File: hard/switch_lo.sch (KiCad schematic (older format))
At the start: 4 parts

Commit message: pc format refactor wip
@lukekaese leds still need to be attenuated
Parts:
- gave numbers to parts that had none: 4

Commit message: layouting update
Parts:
- R97: renamed from R99; footprint Resistor_SMD:R_0603_1608Metric -> Resistor_SMD:R_1210_3225Metric
- R98: renamed from R97; footprint Resistor_SMD:R_0603_1608Metric -> Resistor_SMD:R_0402_1005Metric
- R99: renamed from R98; footprint Resistor_SMD:R_0603_1608Metric -> Resistor_SMD:R_0402_1005Metric

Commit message: driver nmos update
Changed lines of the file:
@@
 $Descr A4 11693 8268
 encoding utf-8
-Sheet 36 69
+Sheet 39 69
 Title ""
 Date ""
@@
 AR Path="/6053C67A/DAE5EF41/6879FA6E" Ref="M95"  Part="1"
 AR Path="/6053C67A/DAE5EF45/6879FA6E" Ref="M96"  Part="1"
-F 0 "M65" H 6078 4300 50  0000 L CNN
+F 0 "M68" H 6078 4300 50  0000 L CNN
 F 1 "IRLML0030TRPBF" H 6078 4255 50  0001 L CNN
 F 2 "Package_TO_SOT_SMD:SOT-23" H 6750 4300 50  0001 C CNN
@@
 AR Path="/6053C67A/DAE5EF41/6879FA74" Ref="R189"  Part="1"
 AR Path="/6053C67A/DAE5EF45/6879FA74" Ref="R192"  Part="1"
-F 0 "R99" H 5720 4546 50  0000 L CNN
+F 0 "R108" H 5720 4546 50  0000 L CNN
 F 1 "470K" H 5720 4455 50  0000 L CNN
 F 2 "Resistor_SMD:R_0402_1005Metric" V 5580 4500 50  0001 C CNN
@@
 AR Path="/6053C67A/DAE5EF41/6879FA7A" Ref="R188"  Part="1"
 AR Path="/6053C67A/DAE5EF45/6879FA7A" Ref="R191"  Part="1"
-F 0 "R98" V 5243 4300 50  0000 C CNN
+F 0 "R107" V 5243 4300 50  0000 C CNN
 F 1 "1K8" V 5334 4300 50  0000 C CNN
 F 2 "Resistor_SMD:R_0402_1005Metric" V 5380 4300 50  0001 C CNN
@@
 AR Path="/6053C67A/DAE5EF41/6879FA80" Ref="#PWR0174"  Part="1"
 AR Path="/6053C67A/DAE5EF45/6879FA80" Ref="#PWR0176"  Part="1"
-F 0 "#PWR0114" H 5650 4450 50  0001 C CNN
+F 0 "#PWR0120" H 5650 4450 50  0001 C CNN
 F 1 "GND" H 5655 4527 50  0000 C CNN
 F 2 "" H 5650 4700 50  0001 C CNN
@@
 AR Path="/6053C67A/DAE5EF41/6879FA89" Ref="#PWR0175"  Part="1"
 AR Path="/6053C67A/DAE5EF45/6879FA89" Ref="#PWR0177"  Part="1"
-F 0 "#PWR0115" H 6000 4450 50  0001 C CNN
+F 0 "#PWR0121" H 6000 4450 50  0001 C CNN
 F 1 "GND" H 6005 4527 50  0000 C CNN
 F 2 "" H 6000 4700 50  0001 C CNN
@@
 AR Path="/6053C67A/DAE5EF41/6879FB77" Ref="R187"  Part="1"
 AR Path="/6053C67A/DAE5EF45/6879FB77" Ref="R190"  Part="1"
-F 0 "R97" H 6070 3896 50  0000 L CNN
+F 0 "R106" H 6070 3896 50  0000 L CNN
 F 1 "0R" H 6070 3805 50  0000 L CNN
 F 2 "Resistor_SMD:R_1210_3225Metric" V 5930 3850 50  0001 C CNN

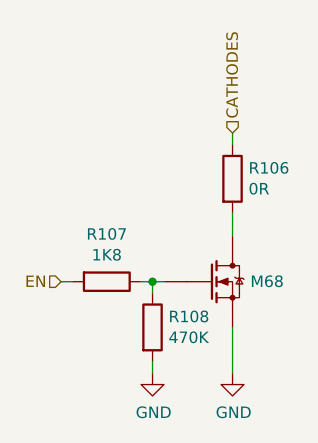
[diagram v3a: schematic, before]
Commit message: uc minimum application
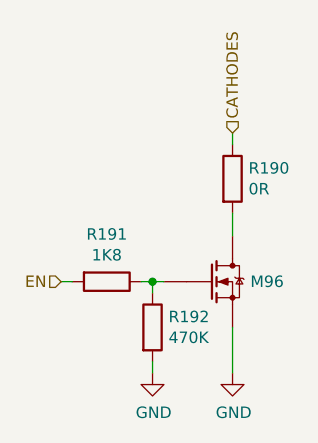
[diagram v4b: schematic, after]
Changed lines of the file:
@@
 $Descr A4 11693 8268
 encoding utf-8
-Sheet 39 69
+Sheet 37 69
 Title ""
 Date ""
@@
 AR Path="/6053C67A/DAE5EF41/6879FA6E" Ref="M95"  Part="1"
 AR Path="/6053C67A/DAE5EF45/6879FA6E" Ref="M96"  Part="1"
-F 0 "M68" H 6078 4300 50  0000 L CNN
+F 0 "M96" H 6078 4300 50  0000 L CNN
 F 1 "IRLML0030TRPBF" H 6078 4255 50  0001 L CNN
 F 2 "Package_TO_SOT_SMD:SOT-23" H 6750 4300 50  0001 C CNN
@@
 AR Path="/6053C67A/DAE5EF41/6879FA74" Ref="R189"  Part="1"
 AR Path="/6053C67A/DAE5EF45/6879FA74" Ref="R192"  Part="1"
-F 0 "R108" H 5720 4546 50  0000 L CNN
+F 0 "R192" H 5720 4546 50  0000 L CNN
 F 1 "470K" H 5720 4455 50  0000 L CNN
 F 2 "Resistor_SMD:R_0402_1005Metric" V 5580 4500 50  0001 C CNN
@@
 AR Path="/6053C67A/DAE5EF41/6879FA7A" Ref="R188"  Part="1"
 AR Path="/6053C67A/DAE5EF45/6879FA7A" Ref="R191"  Part="1"
-F 0 "R107" V 5243 4300 50  0000 C CNN
+F 0 "R191" V 5243 4300 50  0000 C CNN
 F 1 "1K8" V 5334 4300 50  0000 C CNN
 F 2 "Resistor_SMD:R_0402_1005Metric" V 5380 4300 50  0001 C CNN
@@
 AR Path="/6053C67A/DAE5EF41/6879FA80" Ref="#PWR0174"  Part="1"
 AR Path="/6053C67A/DAE5EF45/6879FA80" Ref="#PWR0176"  Part="1"
-F 0 "#PWR0120" H 5650 4450 50  0001 C CNN
+F 0 "#PWR0176" H 5650 4450 50  0001 C CNN
 F 1 "GND" H 5655 4527 50  0000 C CNN
 F 2 "" H 5650 4700 50  0001 C CNN
@@
 AR Path="/6053C67A/DAE5EF41/6879FA89" Ref="#PWR0175"  Part="1"
 AR Path="/6053C67A/DAE5EF45/6879FA89" Ref="#PWR0177"  Part="1"
-F 0 "#PWR0121" H 6000 4450 50  0001 C CNN
+F 0 "#PWR0177" H 6000 4450 50  0001 C CNN
 F 1 "GND" H 6005 4527 50  0000 C CNN
 F 2 "" H 6000 4700 50  0001 C CNN
@@
 AR Path="/6053C67A/DAE5EF41/6879FB77" Ref="R187"  Part="1"
 AR Path="/6053C67A/DAE5EF45/6879FB77" Ref="R190"  Part="1"
-F 0 "R106" H 6070 3896 50  0000 L CNN
+F 0 "R190" H 6070 3896 50  0000 L CNN
 F 1 "0R" H 6070 3805 50  0000 L CNN
 F 2 "Resistor_SMD:R_1210_3225Metric" V 5930 3850 50  0001 C CNN

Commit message: pcb format refactor
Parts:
- renumbered M65 to M66, R97 to R107, R98 to R108, R99 to R109

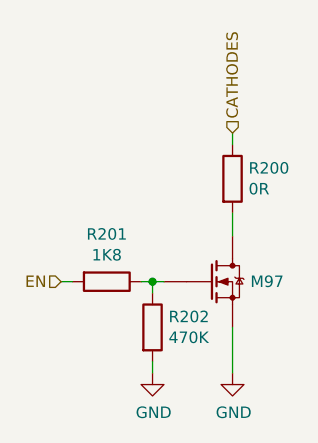
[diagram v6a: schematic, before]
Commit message: general layout update
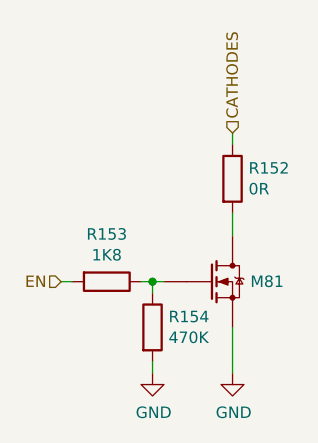
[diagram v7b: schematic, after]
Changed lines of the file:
@@
 $Descr A4 11693 8268
 encoding utf-8
-Sheet 67 69
+Sheet 51 69
 Title ""
 Date ""
@@
 AR Path="/6053C67A/DAE5EF41/6879FA6E" Ref="M96"  Part="1"
 AR Path="/6053C67A/DAE5EF45/6879FA6E" Ref="M97"  Part="1"
-F 0 "M97" H 6078 4300 50  0000 L CNN
+F 0 "M81" H 6078 4300 50  0000 L CNN
 F 1 "IRLML0030TRPBF" H 6078 4255 50  0001 L CNN
 F 2 "Package_TO_SOT_SMD:SOT-23" H 6750 4300 50  0001 C CNN
@@
 AR Path="/6053C67A/DAE5EF41/6879FA74" Ref="R199"  Part="1"
 AR Path="/6053C67A/DAE5EF45/6879FA74" Ref="R202"  Part="1"
-F 0 "R202" H 5720 4546 50  0000 L CNN
+F 0 "R154" H 5720 4546 50  0000 L CNN
 F 1 "470K" H 5720 4455 50  0000 L CNN
 F 2 "Resistor_SMD:R_0402_1005Metric" V 5580 4500 50  0001 C CNN
@@
 AR Path="/6053C67A/DAE5EF41/6879FA7A" Ref="R198"  Part="1"
 AR Path="/6053C67A/DAE5EF45/6879FA7A" Ref="R201"  Part="1"
-F 0 "R201" V 5243 4300 50  0000 C CNN
+F 0 "R153" V 5243 4300 50  0000 C CNN
 F 1 "1K8" V 5334 4300 50  0000 C CNN
 F 2 "Resistor_SMD:R_0402_1005Metric" V 5380 4300 50  0001 C CNN
@@
 AR Path="/6053C67A/DAE5EF41/6879FB77" Ref="R197"  Part="1"
 AR Path="/6053C67A/DAE5EF45/6879FB77" Ref="R200"  Part="1"
-F 0 "R200" H 6070 3896 50  0000 L CNN
+F 0 "R152" H 6070 3896 50  0000 L CNN
 F 1 "0R" H 6070 3805 50  0000 L CNN
 F 2 "Resistor_SMD:R_1210_3225Metric" V 5930 3850 50  0001 C CNN

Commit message: layout process
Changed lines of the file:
@@
 $Descr A4 11693 8268
 encoding utf-8
-Sheet 51 69
+Sheet 52 69
 Title ""
 Date ""
@@
 AR Path="/6053C67A/DAE5EF41/6879FA6E" Ref="M96"  Part="1"
 AR Path="/6053C67A/DAE5EF45/6879FA6E" Ref="M97"  Part="1"
-F 0 "M81" H 6078 4300 50  0000 L CNN
+F 0 "M82" H 6078 4300 50  0000 L CNN
 F 1 "IRLML0030TRPBF" H 6078 4255 50  0001 L CNN
 F 2 "Package_TO_SOT_SMD:SOT-23" H 6750 4300 50  0001 C CNN
@@
 AR Path="/6053C67A/DAE5EF41/6879FA74" Ref="R199"  Part="1"
 AR Path="/6053C67A/DAE5EF45/6879FA74" Ref="R202"  Part="1"
-F 0 "R154" H 5720 4546 50  0000 L CNN
+F 0 "R157" H 5720 4546 50  0000 L CNN
 F 1 "470K" H 5720 4455 50  0000 L CNN
 F 2 "Resistor_SMD:R_0402_1005Metric" V 5580 4500 50  0001 C CNN
@@
 AR Path="/6053C67A/DAE5EF41/6879FA7A" Ref="R198"  Part="1"
 AR Path="/6053C67A/DAE5EF45/6879FA7A" Ref="R201"  Part="1"
-F 0 "R153" V 5243 4300 50  0000 C CNN
+F 0 "R156" V 5243 4300 50  0000 C CNN
 F 1 "1K8" V 5334 4300 50  0000 C CNN
 F 2 "Resistor_SMD:R_0402_1005Metric" V 5380 4300 50  0001 C CNN
@@
 AR Path="/6053C67A/DAE5EF41/6879FA80" Ref="#PWR0183"  Part="1"
 AR Path="/6053C67A/DAE5EF45/6879FA80" Ref="#PWR0185"  Part="1"
-F 0 "#PWR0185" H 5650 4450 50  0001 C CNN
+F 0 "#PWR0155" H 5650 4450 50  0001 C CNN
 F 1 "GND" H 5655 4527 50  0000 C CNN
 F 2 "" H 5650 4700 50  0001 C CNN
@@
 AR Path="/6053C67A/DAE5EF41/6879FA89" Ref="#PWR0184"  Part="1"
 AR Path="/6053C67A/DAE5EF45/6879FA89" Ref="#PWR0186"  Part="1"
-F 0 "#PWR0186" H 6000 4450 50  0001 C CNN
+F 0 "#PWR0156" H 6000 4450 50  0001 C CNN
 F 1 "GND" H 6005 4527 50  0000 C CNN
 F 2 "" H 6000 4700 50  0001 C CNN
@@
 AR Path="/6053C67A/DAE5EF41/6879FB77" Ref="R197"  Part="1"
 AR Path="/6053C67A/DAE5EF45/6879FB77" Ref="R200"  Part="1"
-F 0 "R152" H 6070 3896 50  0000 L CNN
+F 0 "R155" H 6070 3896 50  0000 L CNN
 F 1 "0R" H 6070 3805 50  0000 L CNN
 F 2 "Resistor_SMD:R_1210_3225Metric" V 5930 3850 50  0001 C CNN
